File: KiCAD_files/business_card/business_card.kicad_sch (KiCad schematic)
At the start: 117 parts, among them J2 Conn_01x05_Pin, Q1 AO3401A, SW1 SW_Push, SW2 SW_Push, SW3 SW_Push, U1 STM32U073CCUx, U2 ST25DV04KC-IE6S3

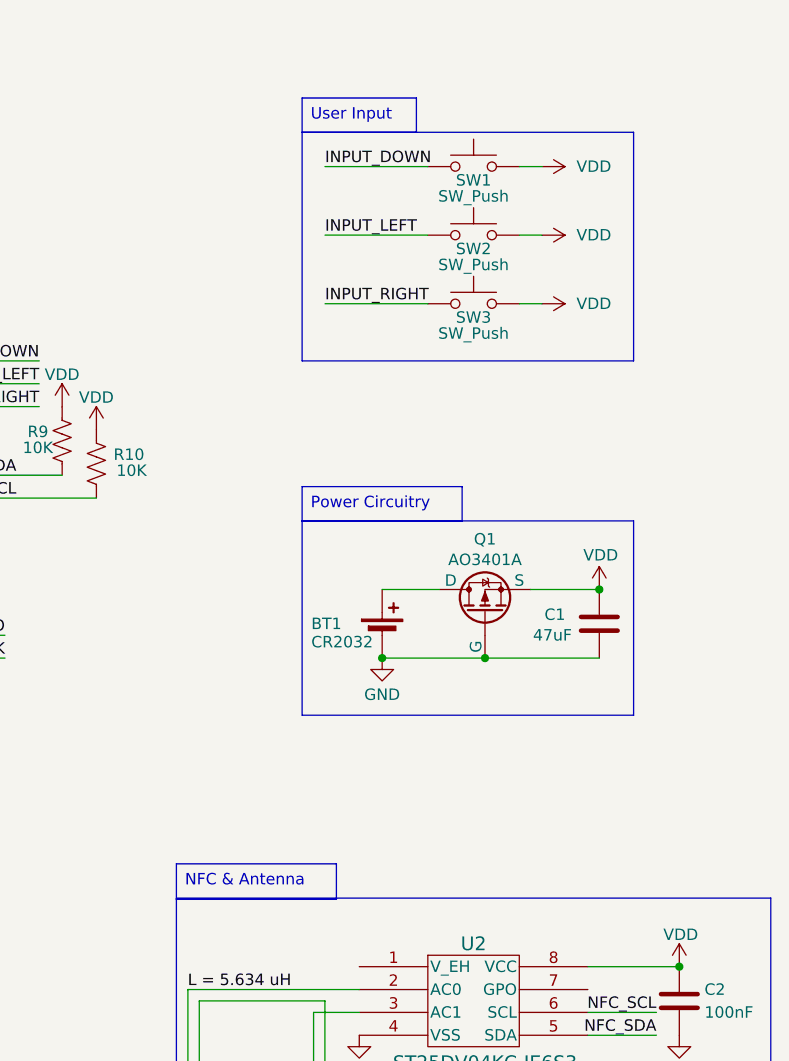
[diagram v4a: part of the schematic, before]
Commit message: Change Button in Schematic and Footprint
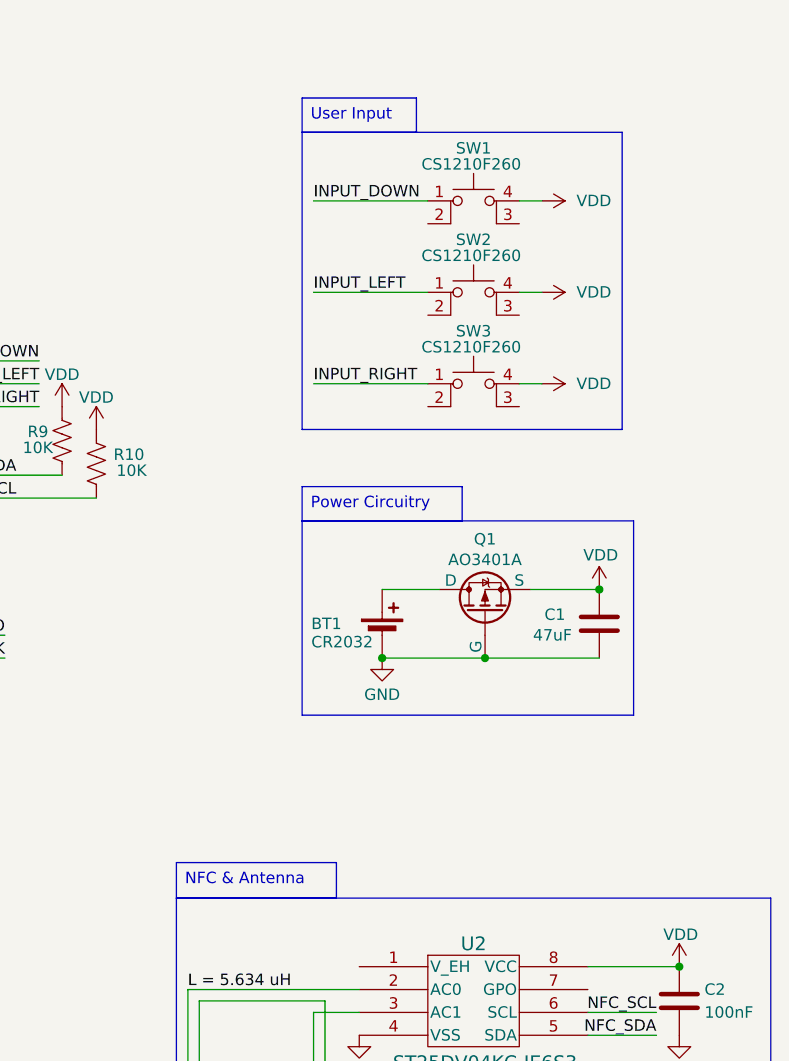
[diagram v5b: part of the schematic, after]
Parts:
- removed SW1, SW2, SW3: SW_Push, TSB008A2526A:TSB008A2526A, symbol Switch:SW_Push
- added SW1, SW2, SW3: CS1210F260, CS1210F260:SW4_CS1210F260_CRS, symbol Switch:SW_MEC_5E
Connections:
- net INPUT_DOWN: now also SW1.1
- net INPUT_LEFT: now also SW2.1
- net INPUT_RIGHT: now also SW3.1
- net VDD: now also SW1.4 (A), SW2.4 (A), SW3.4 (A)

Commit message: Initial Layout for V2.0
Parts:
- removed TP1: VDD, TestPoint:TestPoint_THTPad_D1.0mm_Drill0.5mm, symbol Connector:TestPoint
- removed TP2: GND, TestPoint:TestPoint_THTPad_D1.0mm_Drill0.5mm, symbol Connector:TestPoint
- removed TP3: SDA, TestPoint:TestPoint_THTPad_D1.0mm_Drill0.5mm, symbol Connector:TestPoint
- removed TP4: SCL, TestPoint:TestPoint_THTPad_D1.0mm_Drill0.5mm, symbol Connector:TestPoint
- D1, D10, D11, D12, D13, D14, D15, D16, D17, D18, D19, D2, D20, D21, D22, D23, D24, D25, D26, D27, D28, D29, D3, D30, D31, D32, D33, D34, D35, D36, D37, D38, D39, D4, D40, D41, D42, D43, D44, D45, D46, D47, D48, D49, D5, D50, D51, D52, D53, D54, D55, D56, D57, D58, D59, D6, D60, D61, D62, D63, D64, D65, D66, D67, D68, D69, D7, D70, D71, D72, D73, D74, D75, D76, D77, D78, D79, D8, D80, D81, D82, D83, D84, D9: footprint LED_SMD:LED_0603_1608Metric -> custom_footprints:LED_0603_1608Metric
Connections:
- net COL1: now also U1.46 (PB9); no longer U1.42 (PB6)
- net COL2: now also U1.45 (PB8); no longer U1.43 (PB7)
- net COL3: now also U1.43 (PB7); no longer U1.45 (PB8)
- net COL4: now also U1.42 (PB6); no longer U1.46 (PB9)
- net COL6: now also D25.1 (K)
- net GND: now also J2.1 (Pin_1); no longer J2.5 (Pin_5)
- net INPUT_DOWN: now also SW1.2, U1.31 (PA10); no longer SW1.1, U1.11 (PA1)
- net INPUT_LEFT: now also SW2.2, U1.30 (PA9); no longer SW2.1, U1.12 (PA2)
- net INPUT_RIGHT: now also SW3.2, U1.29 (PA8); no longer SW3.1, U1.13 (PA3)
- net NRST: now also J2.2 (Pin_2); no longer J2.3 (Pin_3)
- net ROW1: now also U1.18 (PB0); no longer U1.41 (PB5)
- net ROW2: now also U1.19 (PB1); no longer U1.40 (PB4)
- net ROW3: now also U1.20 (PB2); no longer U1.39 (PB3)
- net ROW4: now also U1.39 (PB3); no longer U1.20 (PB2)
- net ROW5: now also U1.40 (PB4); no longer U1.19 (PB1)
- net ROW6: now also U1.41 (PB5); no longer U1.18 (PB0)
- net SWCLK: now also J2.3 (Pin_3); no longer J2.4 (Pin_4)
- net SWDIO: now also J2.4 (Pin_4); no longer J2.2 (Pin_2)
- net VDD: now also J2.5 (Pin_5), SW1.3 (K), SW2.3 (K); no longer J2.1 (Pin_1), SW2.4 (A)

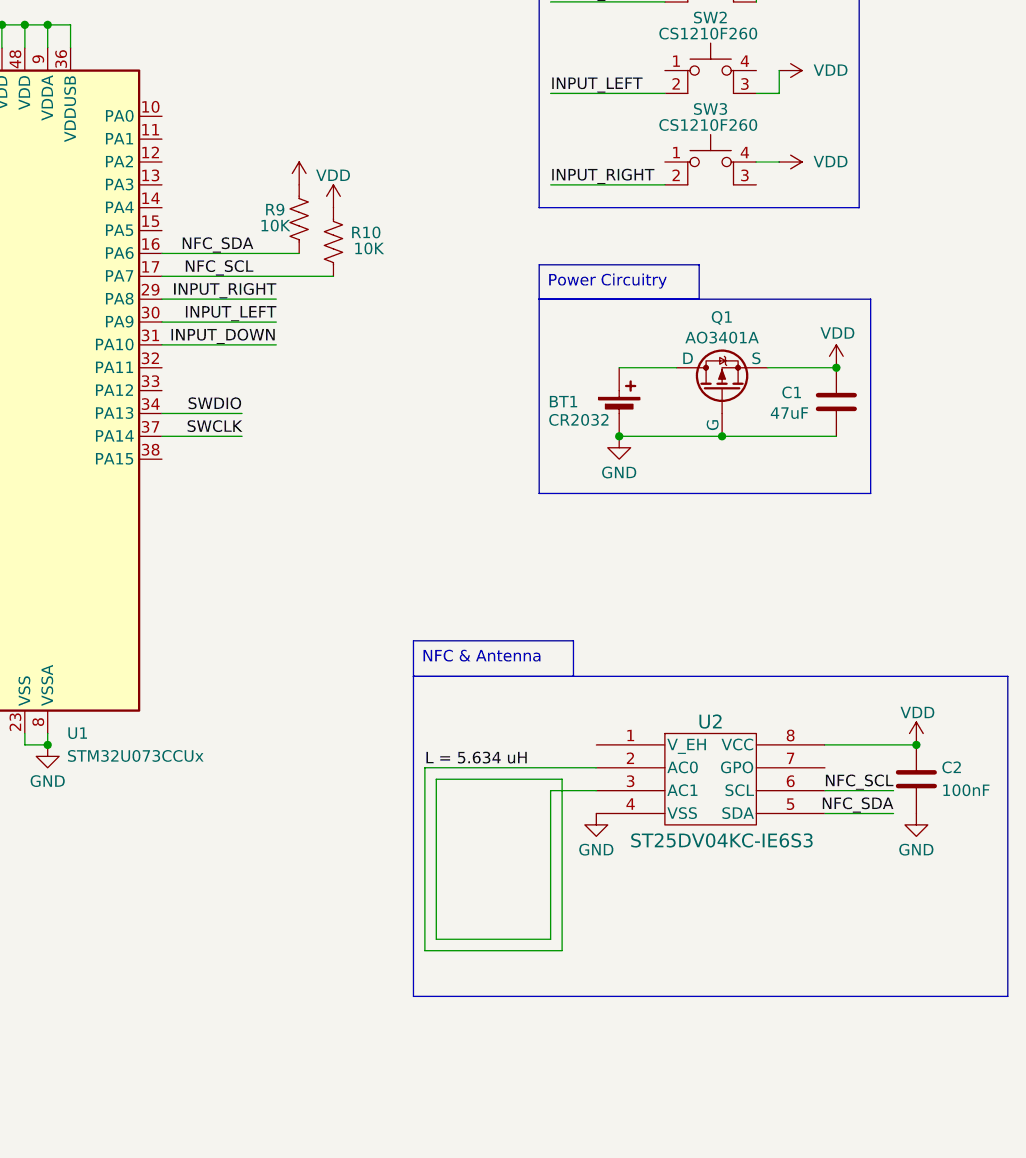
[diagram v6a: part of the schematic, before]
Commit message: Add NFC Antenna
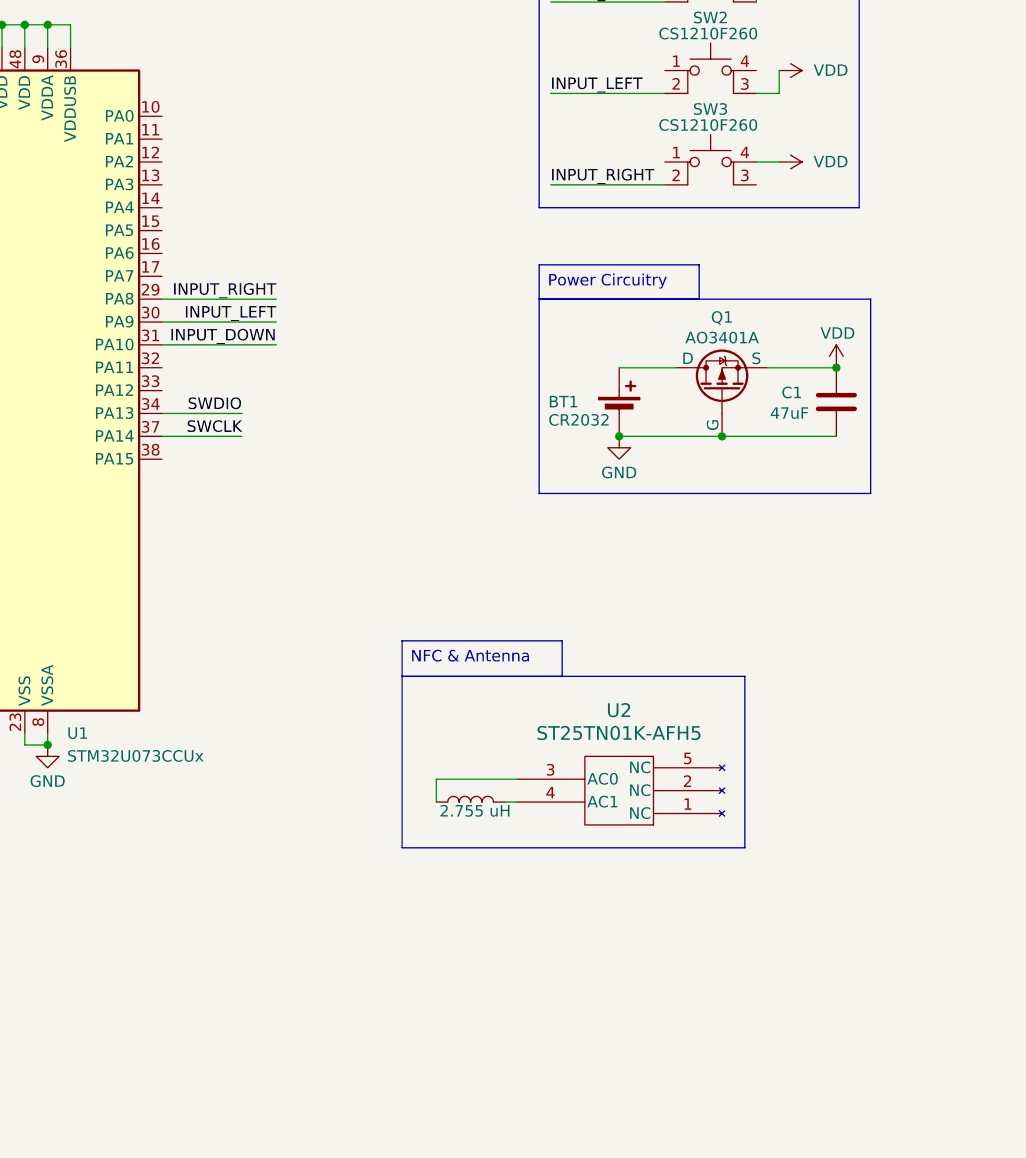
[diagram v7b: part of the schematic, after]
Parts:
- removed C2: 100nF, Capacitor_SMD:C_0603_1608Metric, symbol Device:C
- removed R10, R9: 10K, Resistor_SMD:R_0603_1608Metric, symbol Device:R_US
- removed U2: ST25DV04KC-IE6S3, SO-8_STM, symbol 2026-05-02_23-29-46:ST25DV04KC-IE6S3
- added L1: 2.755 uH, Antenna:25X48MM_NFC, symbol Device:L
- added U2: ST25TN01K-AFH5, UFDFPN-5_1P8X1P5_STM, symbol 2026-05-05_18-10-22:ST25TN01K-AFH5
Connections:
- net NFC_SCL: no longer names the net of U1.17 (PA7)
- net NFC_SDA: no longer names the net of U1.16 (PA6)
- new net: L1.1, U2.3 (AC0)
- new net: L1.2, U2.4 (AC1)

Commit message: Add Mouse Bites to Isolate Tooling Holes
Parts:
- added H3, H4: MountingHole, MountingHole:ToolingHole_1.152mm, symbol Mechanical:MountingHole
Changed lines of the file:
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@@
 	)
 	(symbol
+		(lib_id "Mechanical:MountingHole")
+		(at 22.86 77.47 0)
+		(unit 1)
+		(body_style 1)
+		(exclude_from_sim no)
+		(in_bom no)
+		(on_board yes)
+		(in_pos_files yes)
+		(dnp no)
+		(fields_autoplaced yes)
+		(property "Reference" "H3"
+			(at 25.4 76.1999 0)
+			(show_name no)
+			(do_not_autoplace no)
+			(effects
+				(font
+					(size 1.27 1.27)
+				)
+				(justify left)
+			)
+		)
+		(property "Value" "MountingHole"
+			(at 25.4 78.7399 0)
+			(show_name no)
+			(do_not_autoplace no)
+			(effects
+				(font
+					(size 1.27 1.27)
+				)
+				(justify left)
+			)
+		)
+		(property "Footprint" "MountingHole:ToolingHole_1.152mm"
+			(at 22.86 77.47 0)
+			(hide yes)
+			(show_name no)
+			(do_not_autoplace no)
+			(effects
+				(font
+					(size 1.27 1.27)
+				)
+			)
+		)
+		(property "Datasheet" ""
+			(at 22.86 77.47 0)
+			(hide yes)
+			(show_name no)
+			(do_not_autoplace no)
+			(effects
+				(font
+					(size 1.27 1.27)
+				)
+			)
+		)
+		(property "Description" "Mounting Hole without connection"
+			(at 22.86 77.47 0)
+			(hide yes)
+			(show_name no)
+			(do_not_autoplace no)
+			(effects
+				(font
+					(size 1.27 1.27)
+				)
+			)
+		)
+		(instances
+			(project "business_card"
+				(path "/16d1a3fe-4f2d-4eb3-9740-21c0af2e4feb"
+					(reference "H3")
+					(unit 1)
+				)
+			)
+		)
+	)
+	(symbol
 		(lib_id "Device:LED")
 		(at 81.28 125.73 90)
@@
 					(unit 1)
 				)
+			)
+		)
+	)
+	(symbol
+		(lib_id "Mechanical:MountingHole")
+		(at 22.86 83.82 0)
+		(unit 1)
+		(body_style 1)
+		(exclude_from_sim no)
+		(in_bom no)
+		(on_board yes)
+		(in_pos_files yes)
+		(dnp no)
+		(fields_autoplaced yes)
+		(property "Reference" "H4"
+			(at 25.4 82.5499 0)
+			(show_name no)
+			(do_not_autoplace no)
+			(effects
+				(font
+					(size 1.27 1.27)
+				)
+				(justify left)
+			)
+		)
+		(property "Value" "MountingHole"
+			(at 25.4 85.0899 0)
+			(show_name no)
+			(do_not_autoplace no)
+			(effects
+				(font
+					(size 1.27 1.27)
+				)
+				(justify left)
+			)
+		)
+		(property "Footprint" "MountingHole:ToolingHole_1.152mm"
+			(at 22.86 83.82 0)
+			(hide yes)
+			(show_name no)
+			(do_not_autoplace no)
+			(effects
+				(font
+					(size 1.27 1.27)
+				)
+			)
+		)
+		(property "Datasheet" ""
+			(at 22.86 83.82 0)
+			(hide yes)
+			(show_name no)
+			(do_not_autoplace no)
+			(effects
+				(font
+					(size 1.27 1.27)
+				)
+			)
+		)
+		(property "Description" "Mounting Hole without connection"
+			(at 22.86 83.82 0)
+			(hide yes)
+			(show_name no)
+			(do_not_autoplace no)
+			(effects
+				(font
+					(size 1.27 1.27)
+				)
+			)
+		)
+		(instances
+			(project "business_card"
+				(path "/16d1a3fe-4f2d-4eb3-9740-21c0af2e4feb"
+					(reference "H4")
+					(unit 1)
+				)
